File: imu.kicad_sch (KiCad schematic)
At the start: 6 parts, among them U12 MPU-9250

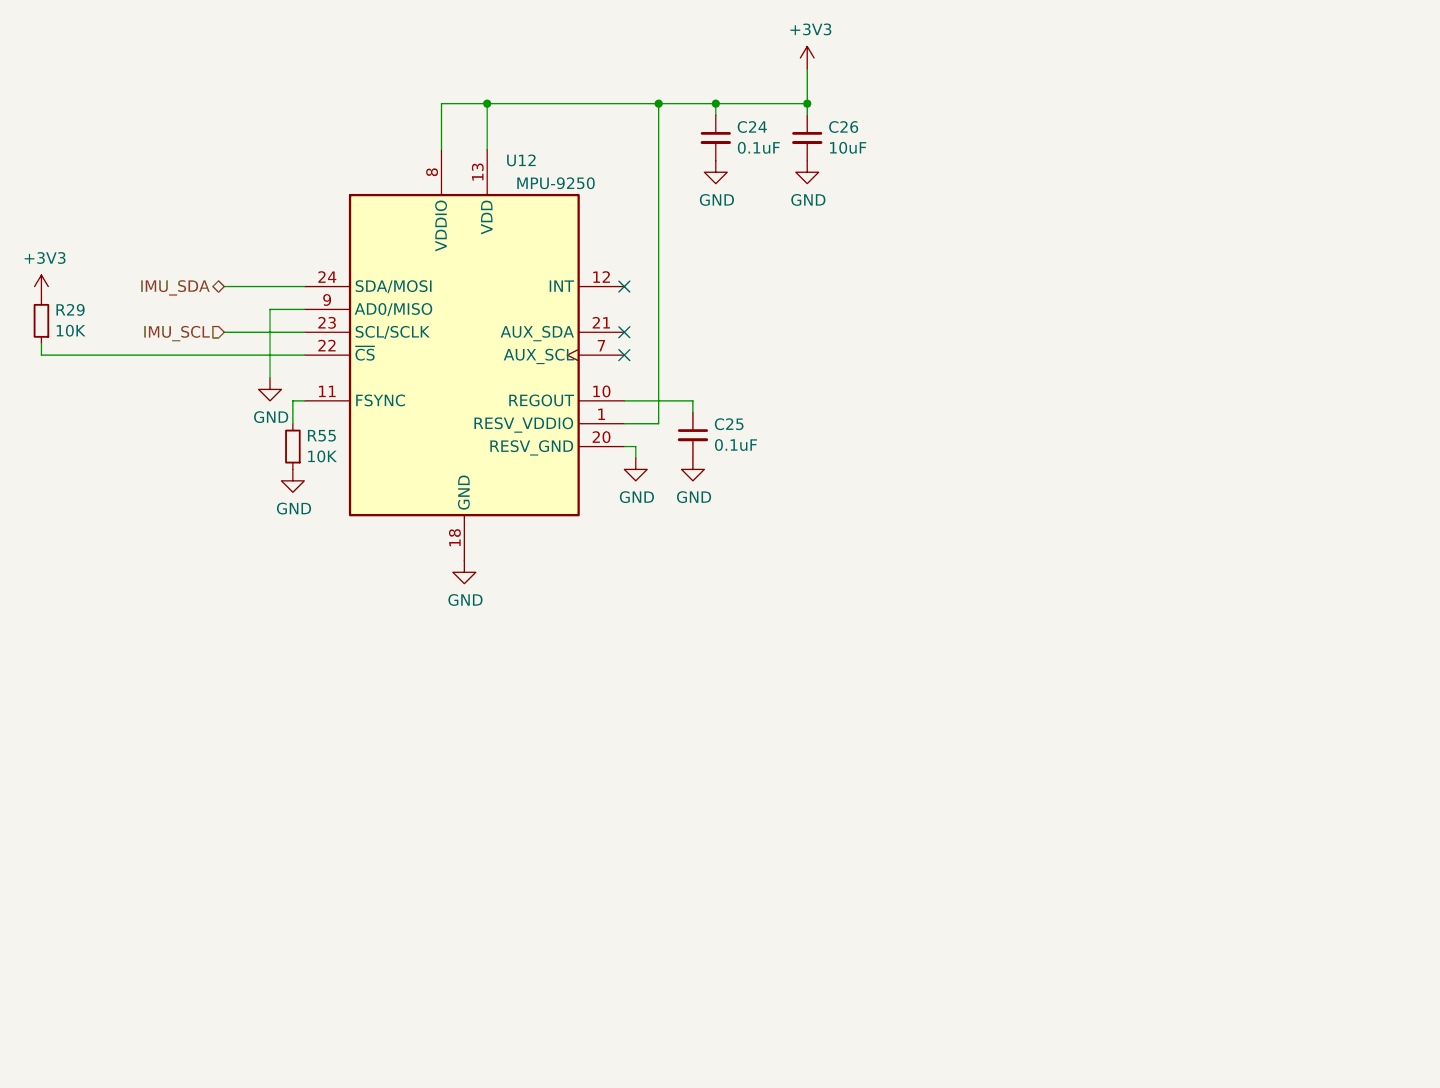
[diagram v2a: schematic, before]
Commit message: Change IMU to BNO055
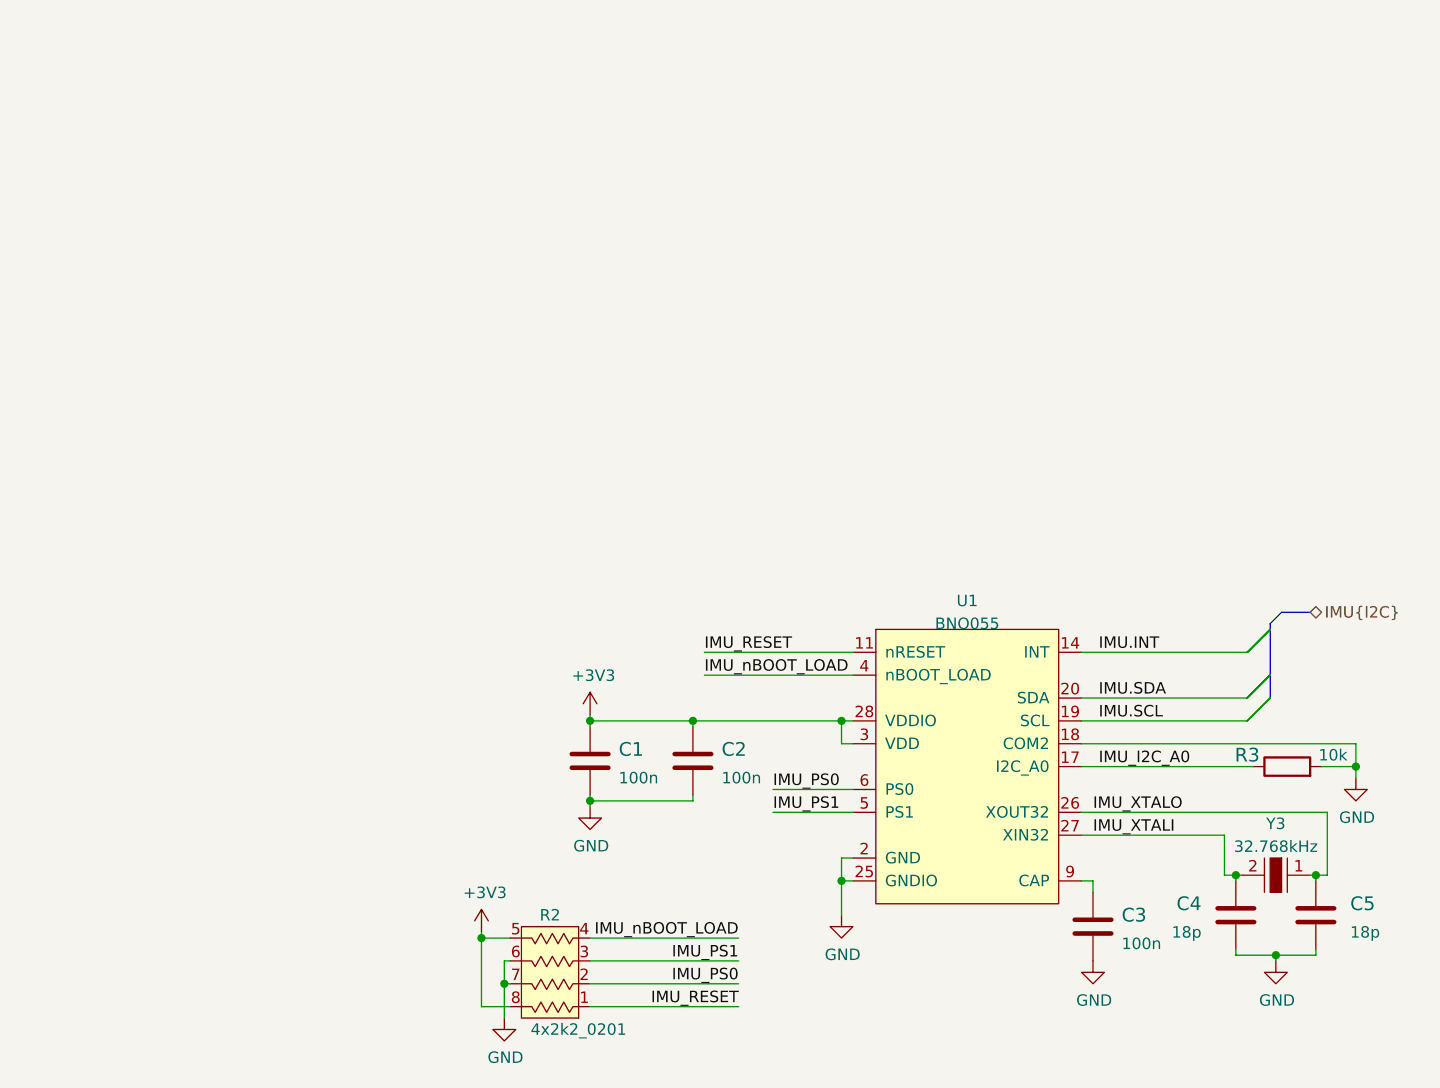
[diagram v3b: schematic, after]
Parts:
- removed C24, C25: 0.1uF, Capacitor_SMD:C_0402_1005Metric, symbol Device:C_Small
- removed C26: 10uF, Capacitor_SMD:C_0603_1608Metric, symbol Device:C_Small
- removed R29, R55: 10K, Resistor_SMD:R_0402_1005Metric, symbol Device:R_Small
- removed U12: MPU-9250, Sensor_Motion:InvenSense_QFN-24_3x3mm_P0.4mm, symbol Sensor_Motion:MPU-9250
- added C1, C2, C3: C_100n_0402, antmicro-footprints:0402-cap, symbol antmicroCapacitors0402:C_100n_0402
- added C4, C5: C_18p_0402, antmicro-footprints:0402-cap, symbol antmicroCapacitors0402:C_18p_0402
- added R2: 4x10k_0201_array, antmicro-footprints:EXB18V, symbol antmicroResistorNetworksArrays:4x10k_0201_array
- added R3: R_10k_0402, antmicro-footprints:0402-res, symbol antmicroResistors0402:R_10k_0402
- added U1: BNO055, antmicro-footprints:LGA-28_5.2x3.8mm_BNO0055, symbol antmicroMotionSensorsIMUsInertialMeasurementUnits:BNO055
- added Y3: ECS-_327-12_5-34B-TR, antmicro-footprints:SMD-2_3.2x1.5mm, symbol antmicroCrystals:ECS-_327-12_5-34B-TR
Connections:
- net +3V3: now also C1.1, C2.1, R2.5, R2.8, U1.28 (VDDIO), U1.3 (VDD)
- net GND: now also C1.2, C2.2, C3.2, C4.2, C5.2, R2.6, R2.7, R3.2, U1.10 (PIN10), U1.15 (PIN15), U1.16 (PIN16), U1.18 (COM2), U1.2 (GND), U1.25 (GNDIO)
- new net: C3.1, U1.9 (CAP)
- new net IMU.INT: U1.14 (INT)
- new net IMU.SCL: U1.19 (COM1)
- new net IMU.SDA: U1.20 (COM0)
- new net IMU_I2C_A0: R3.1, U1.17 (COM3)
- new net IMU_PS0: R2.2, U1.6 (PS0)
- new net IMU_PS1: R2.3, U1.5 (PS1)
- new net IMU_RESET: R2.1, U1.11 (nRESET)
- new net IMU_XTALI: C4.1, U1.27 (XIN32), Y3.2
- new net IMU_XTALO: C5.1, U1.26 (XOUT32), Y3.1
- new net IMU_nBOOT_LOAD: R2.4, U1.4 (nBOOT_LOAD)
- no-connect marks 3 -> 0

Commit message: Loclib, cleanup
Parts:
- C1, C2, C3: footprint antmicro-footprints:0402-cap -> synermycha-electronics-footprints:0402-cap; symbol antmicroCapacitors0402:C_100n_0402 -> synermycha-electronics:C_100n_0402
- C4, C5: footprint antmicro-footprints:0402-cap -> synermycha-electronics-footprints:0402-cap; symbol antmicroCapacitors0402:C_18p_0402 -> synermycha-electronics:C_18p_0402
- R2: footprint antmicro-footprints:EXB18V -> synermycha-electronics-footprints:EXB18V; symbol antmicroResistorNetworksArrays:4x10k_0201_array -> synermycha-electronics:4x10k_0201_array
- R3: footprint antmicro-footprints:0402-res -> synermycha-electronics-footprints:0402-res; symbol antmicroResistors0402:R_10k_0402 -> synermycha-electronics:R_10k_0402
- U1: footprint antmicro-footprints:LGA-28_5.2x3.8mm_BNO0055 -> synermycha-electronics-footprints:LGA-28_5.2x3.8mm_BNO0055; symbol antmicroMotionSensorsIMUsInertialMeasurementUnits:BNO055 -> synermycha-electronics:BNO055
- Y3: footprint antmicro-footprints:SMD-2_3.2x1.5mm -> synermycha-electronics-footprints:SMD-2_3.2x1.5mm; symbol antmicroCrystals:ECS-_327-12_5-34B-TR -> synermycha-electronics:ECS-_327-12_5-34B-TR
